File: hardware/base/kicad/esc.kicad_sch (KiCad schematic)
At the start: 69 parts, among them J3 HY911105AE IN, J4 HY911105AE OUT, U4 LAN9253-I/R4X, U5 TPS3808G33DBVR, U6 M24C16-RMN6TP, U7 TPD4E05U06DQAR, U8 TPD4E05U06DQAR

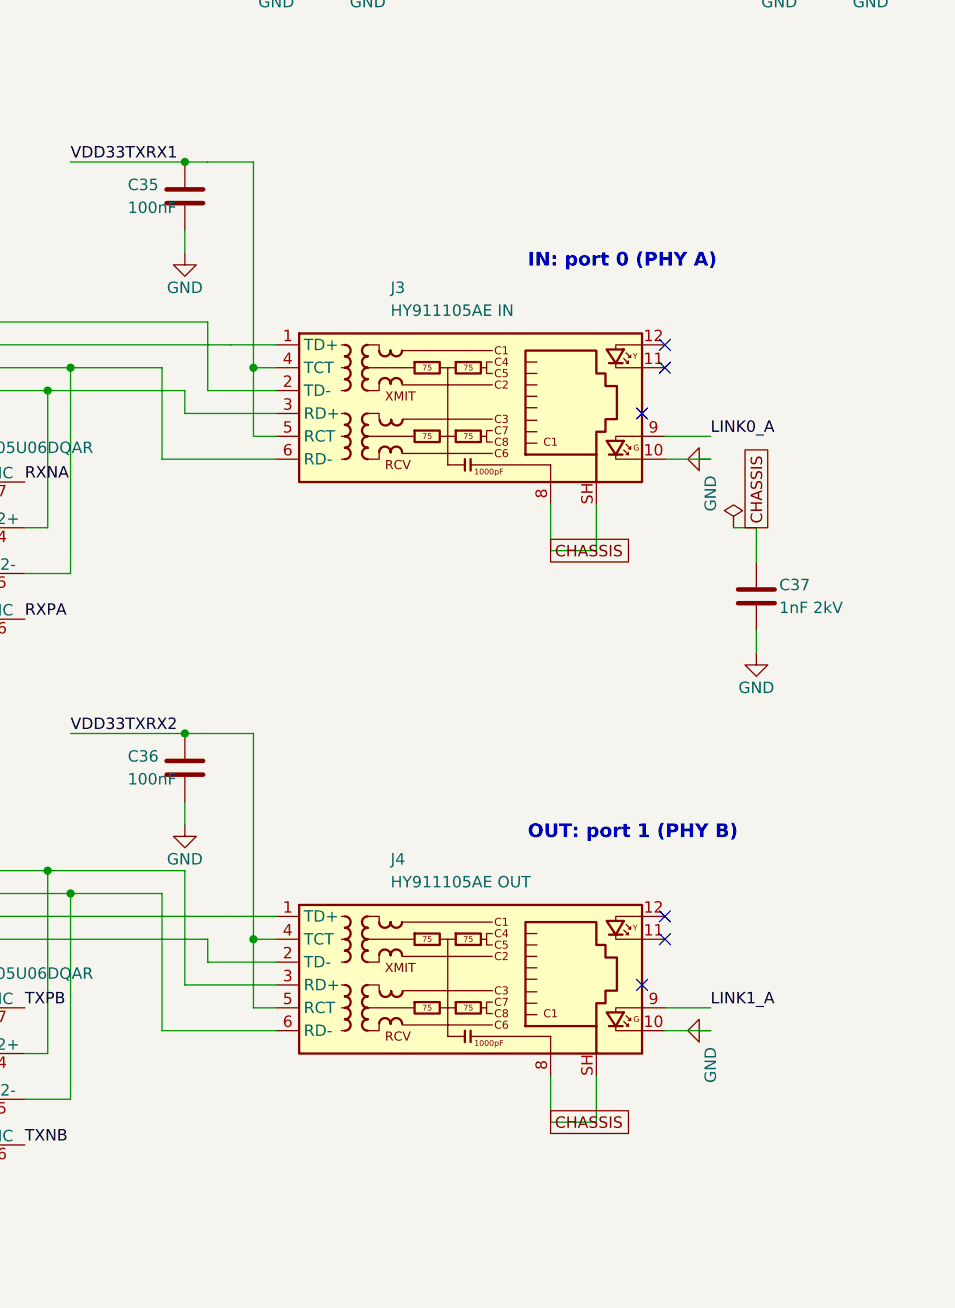
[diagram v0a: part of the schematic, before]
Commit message: Pairs laid in the block layout: arrays on the way, wiring searched, ICs step back, lanes kept; isolated region of the Modbus bus side; supply planes drawn from the placement; pcb.py takes the floor plan
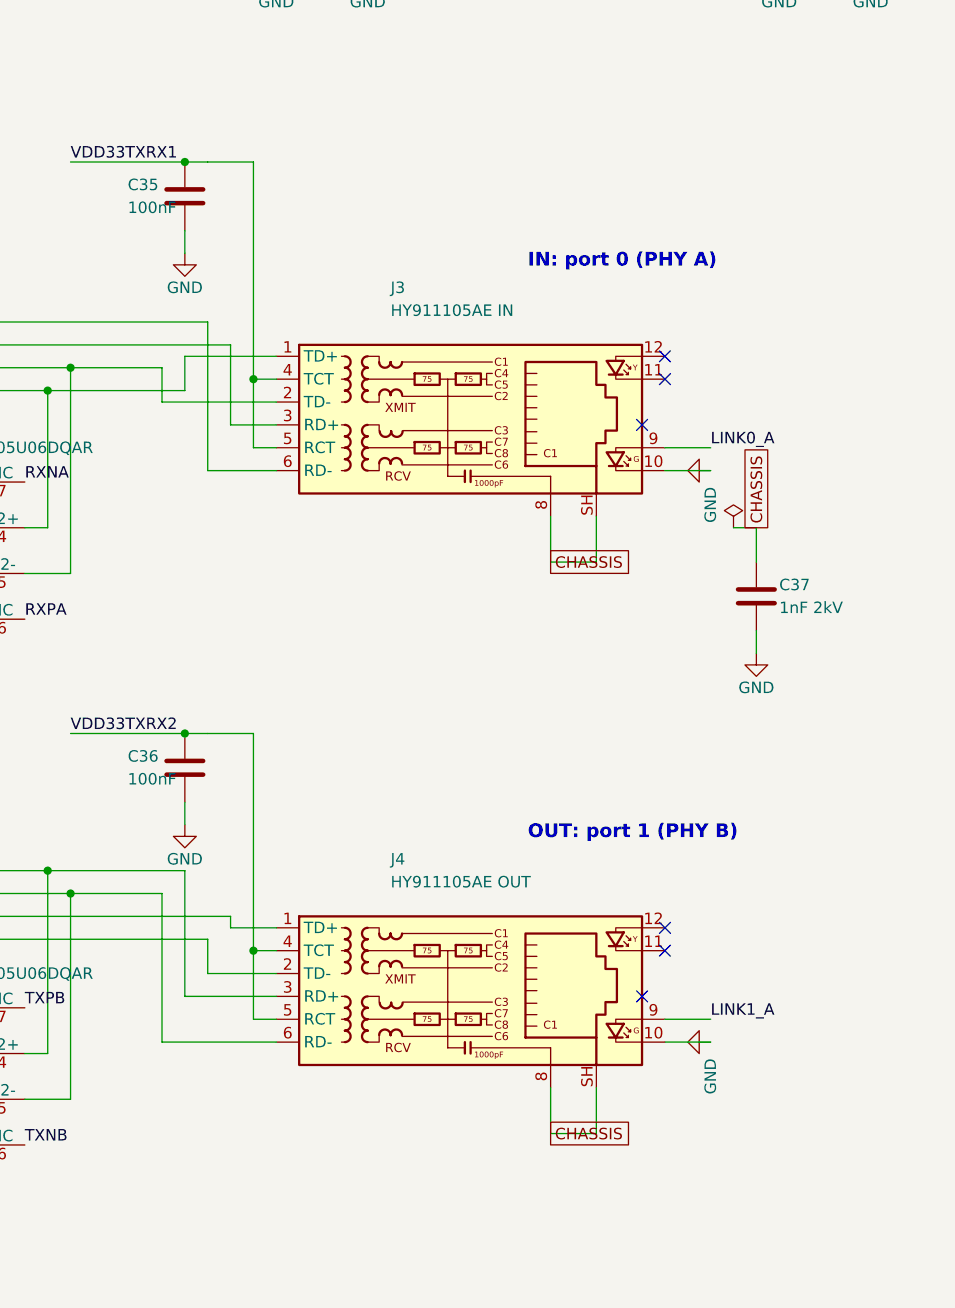
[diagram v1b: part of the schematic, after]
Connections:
- net RXNA: now also J3.1 (TD+); no longer J3.3 (RD+)
- net RXPA: now also J3.2 (TD-); no longer J3.6 (RD-)
- net TXNA: now also J3.3 (RD+); no longer J3.1 (TD+)
- net TXPA: now also J3.6 (RD-); no longer J3.2 (TD-)
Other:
- moved on the sheet: J3, J4

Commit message: Pairs kept from the block layout to the board, their terminations placed with them; tracks laid are an obstacle for every part; wiring of the block layouts checked against the schematic; fixed hash seed for reproducible runs
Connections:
- net RXNA: now also J3.3 (RD+), U7.2 (D1-), U7.9 (NC); no longer J3.1 (TD+), U7.4 (D2+), U7.7 (NC)
- net RXPA: now also J3.6 (RD-), U7.1 (D1+), U7.10 (NC); no longer J3.2 (TD-), U7.5 (D2-), U7.6 (NC)
- net TXNA: now also J3.1 (TD+), U7.5 (D2-), U7.6 (NC); no longer J3.3 (RD+), U7.1 (D1+), U7.10 (NC)
- net TXPA: now also J3.2 (TD-), U7.4 (D2+), U7.7 (NC); no longer J3.6 (RD-), U7.2 (D1-), U7.9 (NC)

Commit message: Modbus termination always fitted (R246, removed for a master in the middle of the line); no ESD array on NRST; Ethernet line nets named TXA_P/TXA_N so that tools pair them
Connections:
- net RXNA renamed RXA_N
- net RXNB renamed RXB_N
- net RXPA renamed RXA_P
- net RXPB renamed RXB_P
- net TXNA renamed TXA_N
- net TXNB renamed TXB_N
- net TXPA renamed TXA_P
- net TXPB renamed TXB_P

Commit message: Base: pin swaps of the placed board (chip selects, step/dir/enable channels, encoder timers 0 and 1, ribbon and Ethernet A ESD channels)
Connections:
- net TXA_N: now also U7.4 (D2+), U7.7 (NC); no longer U7.5 (D2-), U7.6 (NC)
- net TXA_P: now also U7.5 (D2-), U7.6 (NC); no longer U7.4 (D2+), U7.7 (NC)
